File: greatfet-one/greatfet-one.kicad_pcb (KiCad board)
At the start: 4 copper layers, 70.6 x 53.3 mm, 103 parts, among them J1 NEIGHBOR1, J2 NEIGHBOR2, J3 USB-MICRO-B-SHIELDED, J4 USB-MICRO-B-SHIELDED, J5 JTAG, J6 POWER, J7 BONUS_ROW, SW1 DFU, SW2 RESET, U1 LPC4330FBD144, U2 W25Q16DV, U3 AP7333, U4 IP4220CZ6, U5 AP2553W6-7, X1 MCU_XTAL, X2 RTC_XTAL

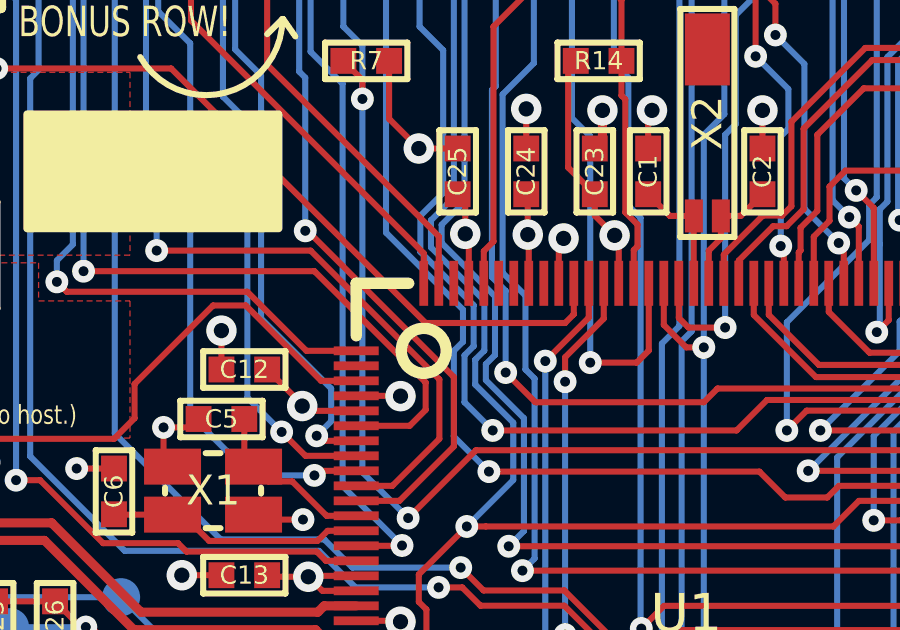
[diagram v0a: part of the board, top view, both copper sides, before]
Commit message: GreatFET One: added ADC pin straps for hardware version detection
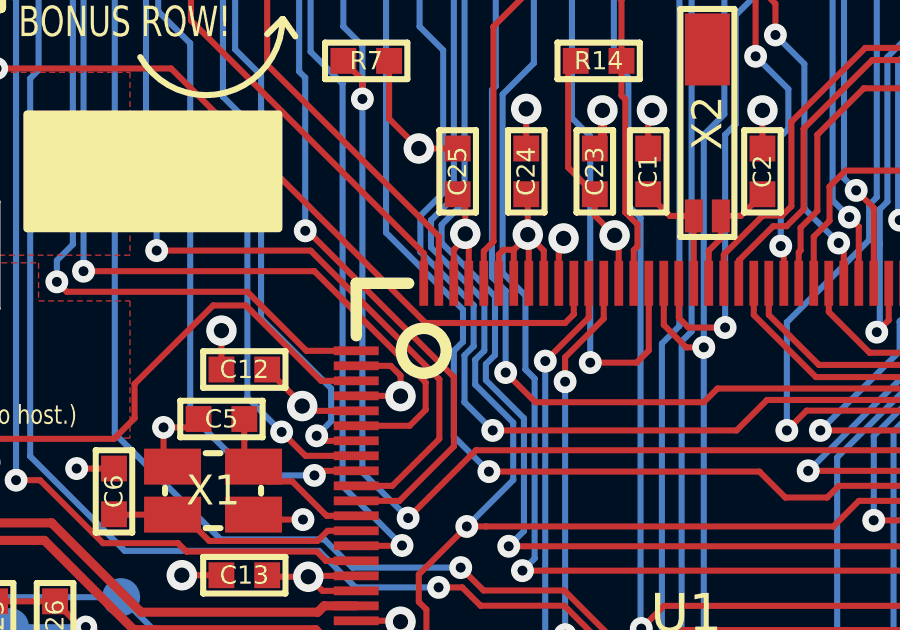
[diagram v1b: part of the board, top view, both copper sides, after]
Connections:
- J5 pad 7: (no net) -> Net-(J5-Pad7)
- U1 pad 136: (no net) -> VCC
- U1 pad 138: (no net) -> VCC
- U1 pad 139: (no net) -> VCC
- U1 pad 142: (no net) -> VCC
- U1 pad 2: (no net) -> GND
- U4 pad 4: (no net) -> Net-(U4-Pad4)
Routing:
- net VCC: track 105.5 -> 112.5 mm
- net GND: track 101.2 -> 103.5 mm
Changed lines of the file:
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@@
 (kicad_pcb (version 4) (host pcbnew 4.0.6)
   (general
-    (links 382)
+    (links 387)
     (no_connects 0)
-    (area 93.424104 68.58 207.466001 127.000001)
+    (area 105.842999 71.044999 176.605001 124.535001)
     (thickness 1.6)
     (drawings 230)
-    (tracks 1569)
+    (tracks 1583)
     (zones 0)
     (modules 103)
-    (nets 134)
+    (nets 136)
   )
   (page A4)
@@
   (net 132 /USB0_VBUS)
   (net 133 /USB0_SENSE)
+  (net 134 "Net-(J5-Pad7)")
+  (net 135 "Net-(U4-Pad4)")
   (net_class Default "This is the default net class."
     (clearance 0.1524)
@@
     (add_net "Net-(J4-Pad2)")
     (add_net "Net-(J4-Pad3)")
+    (add_net "Net-(J5-Pad7)")
     (add_net "Net-(R13-Pad1)")
     (add_net "Net-(R23-Pad2)")
+    (add_net "Net-(U4-Pad4)")
     (add_net VCC)
   )
@@
     (pad 3 smd rect (at 0.95 1.2 180) (size 0.55 0.8) (layers F.Cu F.Paste F.Mask)
       (net 92 /USB0_ID))
-    (pad 4 smd rect (at 0.95 -1.2 180) (size 0.55 0.8) (layers F.Cu F.Paste F.Mask))
+    (pad 4 smd rect (at 0.95 -1.2 180) (size 0.55 0.8) (layers F.Cu F.Paste F.Mask)
+      (net 135 "Net-(U4-Pad4)"))
     (pad 5 smd rect (at 0 -1.2 180) (size 0.55 0.8) (layers F.Cu F.Paste F.Mask)
       (net 132 /USB0_VBUS))
@@
       (net 98 /TDO) (die_length -2147.483648))
     (pad 7 thru_hole circle (at 1.27 0.635) (size 1.0668 1.0668) (drill 0.7112) (layers *.Cu *.Mask)
-      (die_length 0.08128))
+      (net 134 "Net-(J5-Pad7)") (die_length 0.08128))
     (pad 8 thru_hole circle (at 1.27 -0.635) (size 1.0668 1.0668) (drill 0.7112) (layers *.Cu *.Mask)
       (net 99 /TDI) (die_length -2147.483648))
@@
       (net 62 /P4_0) (die_length 0.01524))
     (pad 2 smd rect (at -11.00074 -8.24992) (size 1.50114 0.29464) (layers F.Cu F.Paste F.Mask)
-      (die_length 18.20672))
+      (net 1 GND) (die_length 18.20672))
     (pad 3 smd rect (at -11.00074 -7.74954) (size 1.50114 0.29464) (layers F.Cu F.Paste F.Mask)
       (net 11 /LED2) (die_length 0.01524))
@@
       (net 1 GND) (die_length -2147.483648))
     (pad 136 smd rect (at -4.7498 -11.00074 90) (size 1.50114 0.29464) (layers F.Cu F.Paste F.Mask)
-      (die_length -2147.483648))
+      (net 4 VCC) (die_length -2147.483648))
     (pad 137 smd rect (at -5.25018 -11.00074 90) (size 1.50114 0.29464) (layers F.Cu F.Paste F.Mask)
       (net 4 VCC) (die_length 0.12192))
     (pad 138 smd rect (at -5.75056 -11.00074 90) (size 1.50114 0.29464) (layers F.Cu F.Paste F.Mask)
-      (die_length 0.01524))
+      (net 4 VCC) (die_length 0.01524))
     (pad 139 smd rect (at -6.25094 -11.00074 90) (size 1.50114 0.29464) (layers F.Cu F.Paste F.Mask)
-      (die_length -2147.483648))
+      (net 4 VCC) (die_length -2147.483648))
     (pad 140 smd rect (at -6.74878 -11.00074 90) (size 1.50114 0.29464) (layers F.Cu F.Paste F.Mask)
       (net 63 /P7_7) (die_length -2147.483648))
@@
       (net 4 VCC) (die_length -2147.483648))
     (pad 142 smd rect (at -7.74954 -11.00074 90) (size 1.50114 0.29464) (layers F.Cu F.Paste F.Mask)
-      (die_length 0.01524))
+      (net 4 VCC) (die_length 0.01524))
     (pad 143 smd rect (at -8.24992 -11.00074 90) (size 1.50114 0.29464) (layers F.Cu F.Paste F.Mask)
       (net 104 /ADC0_2) (die_length 18.20672))
@@
   (gr_line (start 172.72 124.46) (end 112.3188 124.46) (angle 90) (layer Edge.Cuts) (width 0.15))
   (gr_line (start 112.3188 71.12) (end 172.72 71.12) (angle 90) (layer Edge.Cuts) (width 0.15))
+  (segment (start 131.23926 92.58808) (end 132.38808 92.58808) (width 0.2032) (layer F.Cu) (net 1))
+  (via (at 132.715 93.599) (size 1.016) (drill 0.508) (layers F.Cu B.Cu) (net 1))
+  (segment (start 132.70484 93.58884) (end 132.715 93.599) (width 0.2032) (layer F.Cu) (net 1))
+  (segment (start 132.70484 93.58884) (end 131.23926 93.58884) (width 0.2032) (layer F.Cu) (net 1) (status 10))
+  (segment (start 132.715 92.915) (end 132.715 93.599) (width 0.2032) (layer F.Cu) (net 1))
+  (segment (start 132.38808 92.58808) (end 132.715 92.915) (width 0.2032) (layer F.Cu) (net 1))
   (segment (start 121.2 101.962) (end 121.5746 102.3366) (width 0.2032) (layer F.Cu) (net 1))
   (segment (start 121.5746 102.3366) (end 122.4534 102.3366) (width 0.2032) (layer F.Cu) (net 1))
@@
   (segment (start 132.68452 101.08692) (end 132.715 101.1174) (width 0.2032) (layer F.Cu) (net 1))
   (via (at 132.715 101.1174) (size 1.016) (drill 0.508) (layers F.Cu B.Cu) (net 1))
-  (segment (start 131.23926 93.58884) (end 132.70484 93.58884) (width 0.2032) (layer F.Cu) (net 1) (status 10))
-  (segment (start 132.70484 93.58884) (end 132.715 93.599) (width 0.2032) (layer F.Cu) (net 1))
-  (via (at 132.715 93.599) (size 1.016) (drill 0.508) (layers F.Cu B.Cu) (net 1))
   (segment (start 137.99058 89.83726) (end 137.99058 88.50122) (width 0.2032) (layer F.Cu) (net 1) (status 10))
   (via (at 138.1506 88.3412) (size 1.016) (drill 0.508) (layers F.Cu B.Cu) (net 1))
@@
   (segment (start 142.48892 89.83726) (end 142.48892 87.59708) (width 0.2032) (layer F.Cu) (net 3) (status 30))
   (segment (start 142.48892 87.59708) (end 142.494 87.592) (width 0.2032) (layer F.Cu) (net 3) (status 30))
+  (segment (start 137.4902 88.7476) (end 136.9568 88.2142) (width 0.2032) (layer F.Cu) (net 4))
+  (segment (start 137.4902 89.83726) (end 137.4902 88.7476) (width 0.2032) (layer F.Cu) (net 4))
+  (via (at 136.9568 88.2142) (size 1.016) (drill 0.508) (layers F.Cu B.Cu) (net 4))
+  (segment (start 135.98906 89.83726) (end 135.98906 88.88094) (width 0.2032) (layer F.Cu) (net 4))
+  (segment (start 136.14944 88.72056) (end 136.48944 88.72056) (width 0.2032) (layer F.Cu) (net 4))
+  (segment (start 135.98906 88.88094) (end 136.14944 88.72056) (width 0.2032) (layer F.Cu) (net 4))
+  (segment (start 136.48944 89.83726) (end 136.48944 88.72056) (width 0.2032) (layer F.Cu) (net 4))
+  (segment (start 136.9568 88.2532) (end 136.9568 88.2142) (width 0.2032) (layer F.Cu) (net 4))
+  (segment (start 136.48944 88.72056) (end 136.9568 88.2532) (width 0.2032) (layer F.Cu) (net 4))
+  (segment (start 134.49046 89.83726) (end 134.49046 88.71954) (width 0.2032) (layer F.Cu) (net 4))
+  (via (at 134.874 88.1888) (size 1.016) (drill 0.508) (layers F.Cu B.Cu) (net 4))
+  (segment (start 134.874 88.336) (end 134.874 88.1888) (width 0.2032) (layer F.Cu) (net 4))
+  (segment (start 134.49046 88.71954) (end 134.874 88.336) (width 0.2032) (layer F.Cu) (net 4))
   (segment (start 118.999 107.823) (end 118.364 107.823) (width 0.2032) (layer F.Cu) (net 4))
   (segment (start 118.364 107.823) (end 117.475 106.934) (width 0.2032) (layer F.Cu) (net 4))
@@
   (via (at 144.526 113.538) (size 1.016) (drill 0.508) (layers F.Cu B.Cu) (net 4))
   (via (at 155.2194 89.1032) (size 1.016) (drill 0.508) (layers F.Cu B.Cu) (net 4))
-  (via (at 136.9568 88.2142) (size 1.016) (drill 0.508) (layers F.Cu B.Cu) (net 4))
-  (via (at 134.874 88.1888) (size 1.016) (drill 0.508) (layers F.Cu B.Cu) (net 4))
   (via (at 155.0416 107.5182) (size 1.016) (drill 0.508) (layers F.Cu B.Cu) (net 4))
   (via (at 144.526 113.538) (size 1.016) (drill 0.508) (layers F.Cu B.Cu) (net 4))
